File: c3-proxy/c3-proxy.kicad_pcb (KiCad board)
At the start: 4 copper layers, 74.8 x 50 mm, 63 parts, among them J1 J-SAMTEC-TFM-120-X1-XXX-D-RA, J2 SFM-120-02-X-DH, J3 USB_C_Receptacle_USB2.0_16P, J4 Barrel_Jack, Q1 DMP2035UQ-7, Q2 DMP2035UQ-7, Q3 DMP2035UQ-7, Q4 DMP2035UQ-7, Q6 31-DMN2053UQ-13CT-ND, SW1 C&K PCM13SMTR, U1 MCP2221AxST, U2 INA226, U3 LTC4412xS6, U4 LTC4412xS6, U5 TS5A21366, U6 MAX892LEUA+T, U7 MIC23050-SYML, U8 LTC4412xS6, U9 IP4234CZ6,125

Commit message: style and logic fixes
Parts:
- removed REF**: Polarity_Center_Positive_6mm_SilkScreen, Symbol:Polarity_Center_Positive_6mm_SilkScreen
- added C7: 100nF, oresat-passives:0805-A, F.Cu at (114.8, 108.8)
- added C8: 1uF, oresat-passives:0603-A, F.Cu at (164.8, 100.8)
- added C9: 1uF, oresat-passives:0603-A, F.Cu at (158.8, 101.5)
- added D13: 1N4151WS, Diode_SMD:D_SOD-323, F.Cu at (110.8, 102.8)
- added D4: GREEN, oresat-passives:0603-A, F.Cu at (140.2, 123.2)
- added Q7: DMP2035UQ-7, Package_TO_SOT_SMD:SOT-23-3, F.Cu at (115.5, 103.0)
- added R7: 10k, oresat-passives:0603-A, F.Cu at (140.2, 119.5)
- added R95: 10k, oresat-passives:0603-C-NOSILK, F.Cu at (113.0, 101.8)
- added TP24: Test-Point, oresat-misc:TestPoint-0.75mm-th, F.Cu at (157.8, 97.0)
- added TP25: Test-Point, oresat-misc:TestPoint-0.75mm-th, F.Cu at (171.5, 99.0)
- added TP26: Test-Point, oresat-misc:TestPoint-0.75mm-th, F.Cu at (115.5, 106.8)
- added TP27: Test-Point, oresat-misc:TestPoint-0.75mm-th, F.Cu at (158.3, 121.6)
- added vCAN: vulCAN, oresat-pcbs:vulCAN, F.Cu at (68.5, 97.9)
- R13, R14: value 1k -> 10k
- moved D1 38.2 mm to (146.5, 123.2), turned to -90 degrees
- moved R5 37.4 mm to (146.5, 119.5), turned to 90 degrees
- moved TP15 3.10 mm to (166.2, 129.5)
- moved D2 1.50 mm to (143.0, 109.8)
- moved R13 1.50 mm to (143.0, 105.7)
- moved D3 0.71 mm to (147.8, 109.8)
- moved R14 0.71 mm to (147.8, 105.8)
- moved U4 0.35 mm to (125.2, 133.5)
- moved TP20 0.13 mm to (120.0, 131.5)
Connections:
- D1 pad 2: /OPD_SCL -> /OPD_PWR
- Q4 pad 3: /OPD_SCL -> /OPD_PWR
- U2 pad 3: unconnected-(U2-~{Alert}-Pad3) -> Net-(Q7-G)
- U5 pad 5: /OPD_PWR -> /OPD_SCL
- U8 pad 6: /OPD_SCL -> /OPD_PWR
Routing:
- net VUSB: track 41.6 -> 15.1 mm, vias 2 -> 11
- net Net-(Q7-G): track 0.00 -> 9.54 mm, vias 0 -> 2
- net 3.3V: track 29.3 -> 34.8 mm, vias 11 -> 17
- net Net-(BZ1--): track 0.00 -> 3.94 mm
- net /OPD_SCL: track 105.3 -> 102.7 mm, vias 3 -> 5
- net /OPD_PWR: track 103.1 -> 105.5 mm, vias 5 -> 3
- net unconnected-(TP24-Pad1): track 0.00 -> 2.09 mm
- net Net-(D4-K): track 0.00 -> 1.95 mm
- net /current sensing/LOCAL_SDA: track 62.4 -> 60.5 mm
- net Net-(D2-A): track 8.66 -> 7.19 mm
- net GND: track 58.8 -> 57.3 mm, vias 180 -> 197
- net Net-(U1-GP3): track 33.9 -> 32.5 mm
- net /current sensing/LOCAL_SCL: track 65.7 -> 66.6 mm
- net Net-(D3-A): track 12.1 -> 12.8 mm
- net Net-(D1-K): track 2.54 -> 1.95 mm
- added copper zone on In2.Cu, net VUSB
- removed copper zone on F.Cu, net VUSB
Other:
- board text added: "3.3V Power"

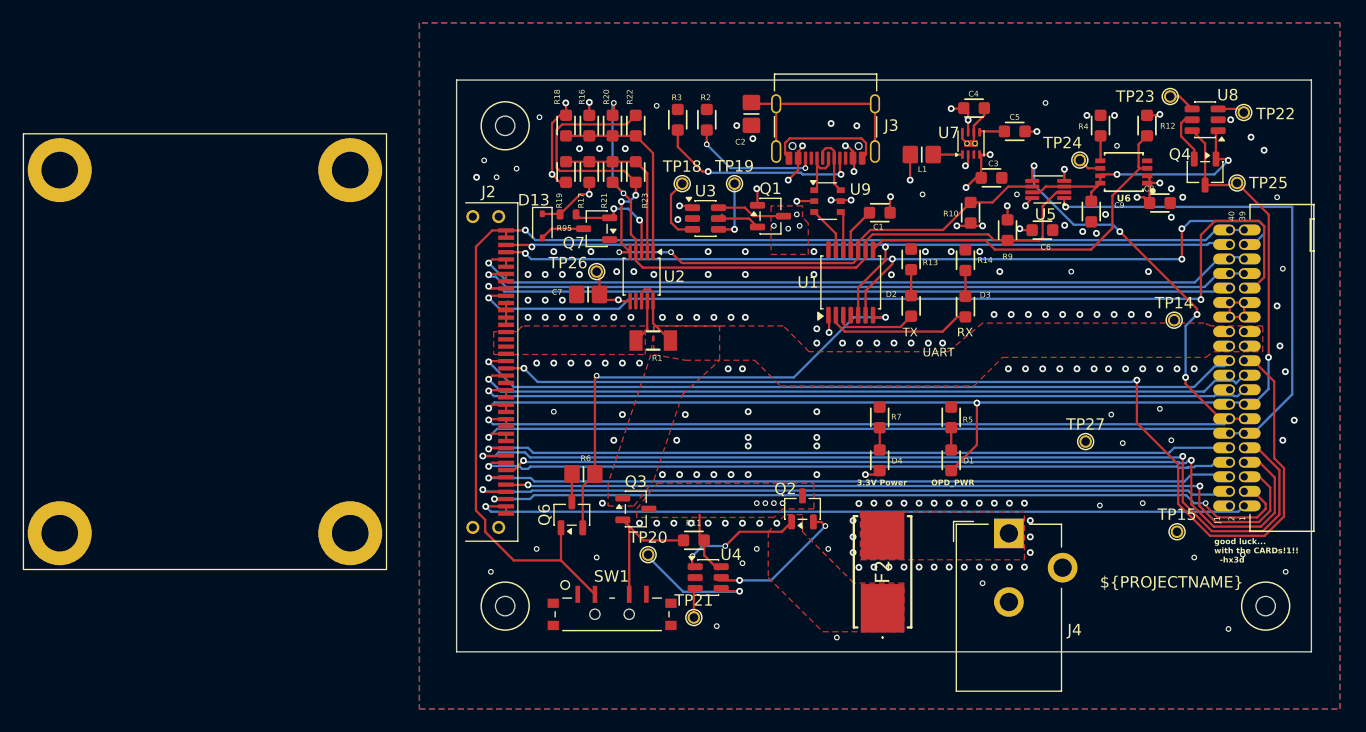
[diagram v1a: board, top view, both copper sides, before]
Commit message: final layout and schematic touch ups
killed buzzer
deleted old folder
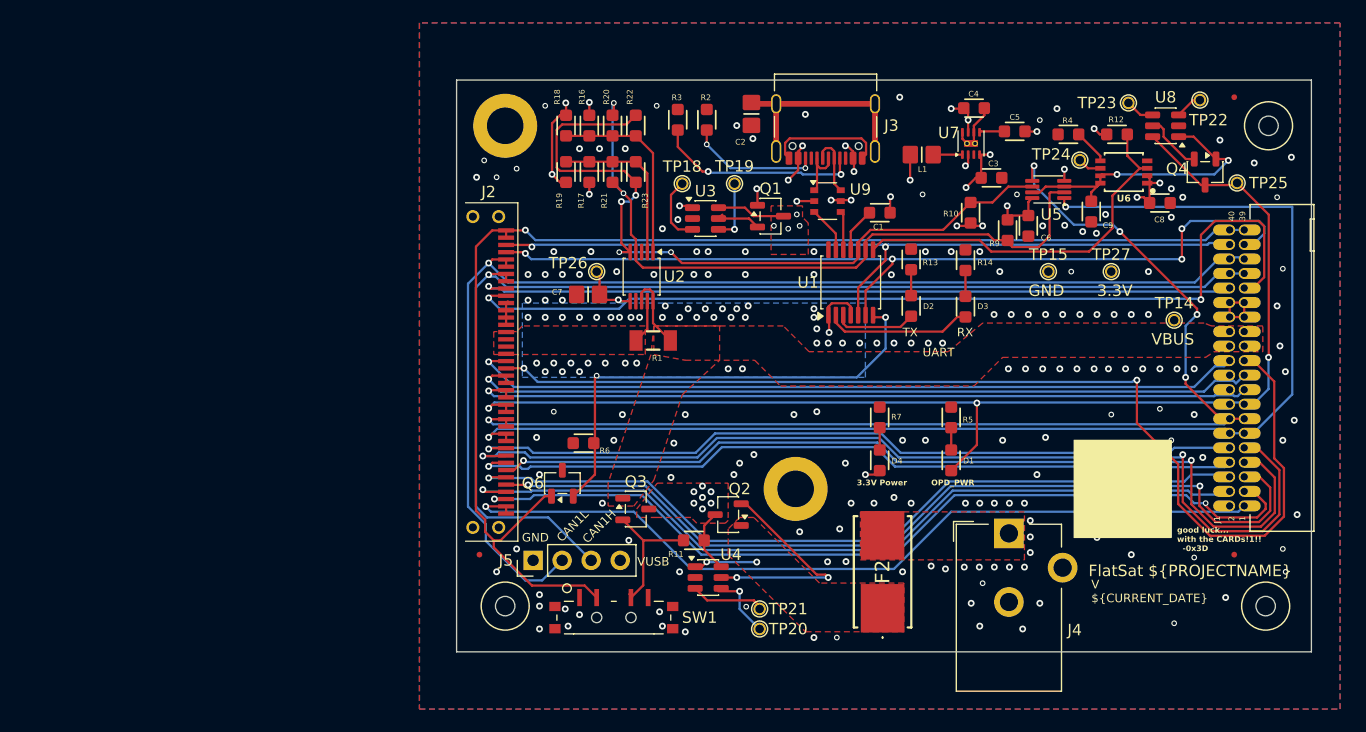
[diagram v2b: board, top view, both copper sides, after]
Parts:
- removed D13: 1N4151WS, Diode_SMD:D_SOD-323
- removed Q7: DMP2035UQ-7, Package_TO_SOT_SMD:SOT-23-3
- removed R95: 10k, oresat-passives:0603-C-NOSILK
- added FID1: Fiducial, Fiducial:Fiducial_0.5mm_Mask1mm, F.Cu at (171.2, 131.5)
- added FID2: Fiducial, Fiducial:Fiducial_0.5mm_Mask1mm, F.Cu at (105.2, 131.5)
- added FID3: Fiducial, Fiducial:Fiducial_0.5mm_Mask1mm, F.Cu at (171.2, 91.5)
- added J5: Conn_01x04, Connector_PinHeader_2.54mm:PinHeader_1x04_P2.54mm_Vertical, F.Cu at (109.9, 132.0)
- C5: value 470uF -> 470pF
- D3: value GRN -> GREEN
- R6: footprint oresat-passives:0805-A -> oresat-passives:0603-A
- moved HW3 66.8 mm to (174.2, 94.0)
- moved vCAN 39.1 mm to (107.5, 94.0)
- moved TP15 25.4 mm to (155.0, 106.8)
- moved TP27 15.0 mm to (160.5, 106.8)
- moved TP20 11.7 mm to (129.8, 138.0)
- moved Q2 6.52 mm to (127.0, 128.0), turned to 180 degrees
- moved TP21 5.80 mm to (129.8, 136.2)
- moved TP22 3.99 mm to (168.2, 91.8)
- moved TP23 3.70 mm to (162.0, 92.0)
- moved U8 3.49 mm to (165.2, 94.0)
- moved R4 2.91 mm to (156.8, 94.8), turned to 180 degrees
- moved Q6 2.89 mm to (112.5, 125.2)
- moved R12 2.73 mm to (161.0, 94.8), turned to 0 degrees
- moved R6 2.71 mm to (114.3, 121.8)
- moved C6 1.29 mm to (153.2, 102.8), turned to -90 degrees
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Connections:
- C2 pad 1: GND -> Net-(J3-SHIELD)
- J3 pad SH: GND -> Net-(J3-SHIELD)
- TP24 pad 1: unconnected-(TP24-Pad1) -> Net-(U6-~{FAULT})
- U1 pad 4: unconnected-(U1-~{RST}-Pad4) -> 3.3V
- U2 pad 3: Net-(Q7-G) -> unconnected-(U2-~{Alert}-Pad3)
- U6 pad 6: unconnected-(TP24-Pad1) -> Net-(U6-~{FAULT})
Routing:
- net /CAN1_L: track 70.0 -> 104.6 mm
- net VUSB: track 15.1 -> 48.7 mm
- net /CAN1_H: track 69.2 -> 101.9 mm
- net GND: track 57.3 -> 35.1 mm, vias 197 -> 202
- net Net-(J3-SHIELD): track 0.00 -> 22.0 mm
- net Net-(Q7-G): track 9.54 -> 0.00 mm, vias 2 -> 0
- net Net-(Q2-G): track 12.5 -> 19.6 mm
- net Net-(Q2-D): track 11.1 -> 5.57 mm
- net Net-(U4-STAT): track 11.3 -> 5.96 mm
- net /~{SD}: track 109.1 -> 113.5 mm
- net /SPARE3: track 72.6 -> 76.9 mm
- net /SPARE5: track 74.4 -> 78.7 mm
- net /SPARE4: track 67.4 -> 71.7 mm
- net /SPARE6: track 66.8 -> 71.1 mm
- net Net-(U4-CTL): track 2.36 -> 6.53 mm
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- added copper zone on B.Cu, net 3.3V
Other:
- board text added: "3.3V"
- board text added: "CAN1H"
- board text added: "CAN1L"
- board text added: "FlatSat ${PROJECTNAME}"
- board text added: "GND"
- board text added: "V${REVISION} ${CURRENT_DATE}"
- board text added: "VBUS"
- board text added: "VUSB"
- board text added: "good luck... with the CARDs!1!! -0x3D"
- board text removed: "${PROJECTNAME}"
- board text removed: "${REVISION}"
- board text removed: "good luck... with the CARDs!1!! -hx3d"

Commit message: deleted the power pal :(, fixed silkscreen
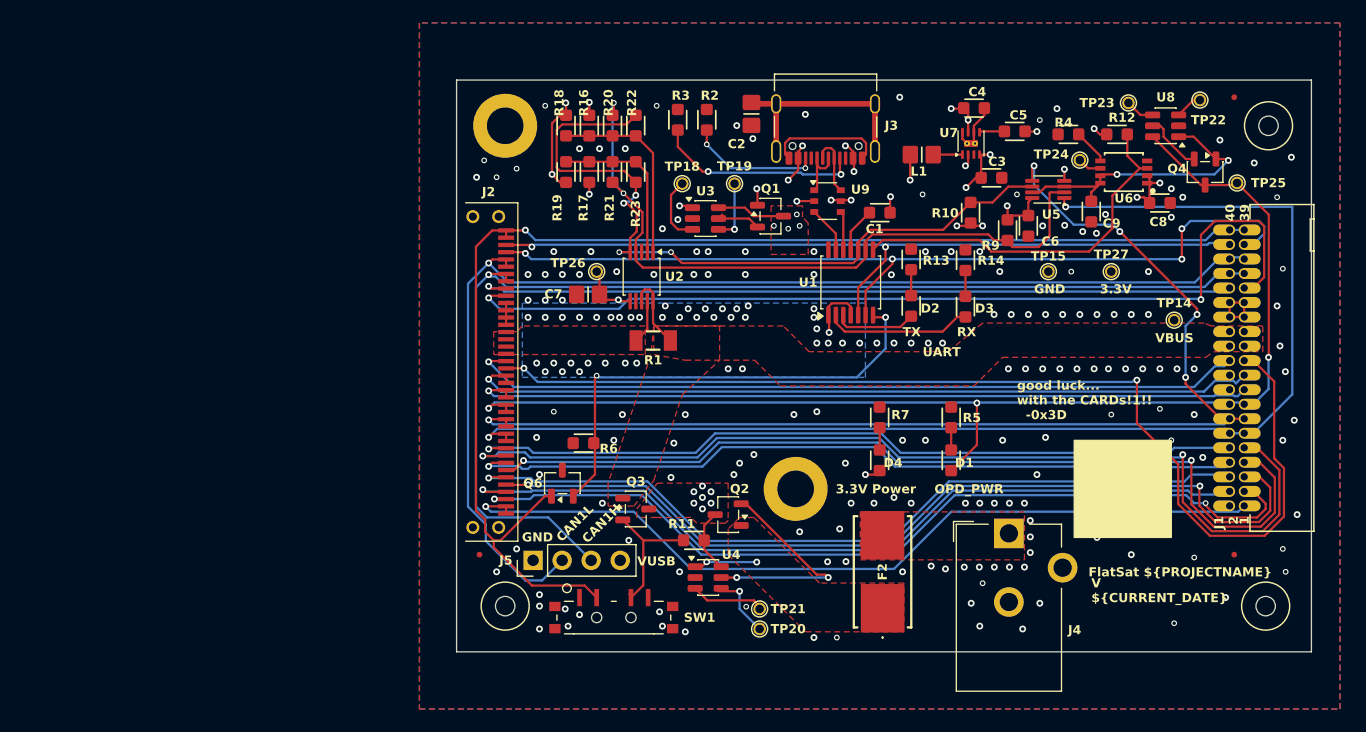
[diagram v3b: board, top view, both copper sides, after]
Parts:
- J2: value SFM-120-02-X-DH -> SFM-120-02-L-DH-TR
- moved G*** 9.54 mm to (142.0, 119.6)
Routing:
- net /OPD_SDA: track 112.0 -> 111.5 mm

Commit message: replaced obsolete resistor
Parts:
- J2: value SFM-120-02-L-DH-TR -> SFM-120-02-X-DH
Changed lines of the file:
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@@
 			)
 		)
-		(property "Datasheet" "https://riedon.com/media/pdf/CSR.pdf"
+		(property "Datasheet" "https://www.vishay.com/docs/30100/wsl.pdf"
 			(at 0 0 0)
 			(layer "F.Fab")
@@
 			)
 		)
-		(property "Description" "10 mOhms ±1% 1W Chip Resistor 1206 (3216 Metric) Current Sense, Non-Inductive Metal Element"
+		(property "Description" "10 mOhms ±1% 0.25W, 1/4W Chip Resistor 1206 (3216 Metric) Anti-Sulfur, Automotive AEC-Q200, Current Sense, Moisture Resistant, Pulse Withstanding Metal Element"
 			(at 0 0 0)
 			(layer "F.Fab")
@@
 			)
 		)
-		(property "DPN" "696-1374-1-ND"
+		(property "DPN" "WSLC-.01TR-ND"
 			(at 0 0 180)
 			(unlocked yes)
@@
 			)
 		)
-		(property "MFR" "Riedon"
+		(property "MFR" "Vishay Dale"
 			(at 0 0 180)
 			(unlocked yes)
@@
 			)
 		)
-		(property "MPN" "CSR1206-0R01F1"
+		(property "MPN" "WSL1206R0100FEA"
 			(at 0 0 180)
 			(unlocked yes)
@@
 			)
 		)
-		(property "KiLib_Generator" "Microchip Technology"
-			(at 0 0 90)
-			(unlocked yes)
-			(layer "F.Fab")
-			(hide yes)
-			(effects
-				(font
-					(size 1 1)
-					(thickness 0.15)
-				)
-			)
-		)
 		(property "DIST" "DigiKey"
 			(at 0 0 90)
@@
 		)
 		(property "MPN" "MIC23050-SYML-TR"
+			(at 0 0 90)
+			(unlocked yes)
+			(layer "F.Fab")
+			(hide yes)
+			(effects
+				(font
+					(size 1 1)
+					(thickness 0.15)
+				)
+			)
+		)
+		(property "MFR" "Microchip Technology"
 			(at 0 0 90)
 			(unlocked yes)
@@
 		(sheetname "/opd/")
 		(sheetfile "measurement.kicad_sch")
+		(units
+			(unit
+				(name "A")
+				(pins "7" "2" "3" "6" "9" "8" "1" "4" "5")
+			)
+		)
 		(attr smd)
 		(duplicate_pad_numbers_are_jumpers no)
@@
 			)
 		)
-		(property "Value" "SFM-120-02-L-DH-TR"
+		(property "Value" "SFM-120-02-X-DH"
 			(at 0 1 90)
 			(unlocked yes)
@@
 		(sheetname "/")
 		(sheetfile "c3-proxy.kicad_sch")
+		(units
+			(unit
+				(name "A")
+				(pins "1" "2" "3" "4" "5" "6" "7" "8" "9" "10" "11" "12" "13" "14" "15"
+					"16" "17" "18" "19" "20" "21" "22" "23" "24" "25" "26" "27" "28" "29"
+					"30" "31" "32" "33" "34" "35" "36" "37" "38" "39" "40"
+				)
+			)
+		)
 		(duplicate_pad_numbers_are_jumpers no)
 		(fp_line
